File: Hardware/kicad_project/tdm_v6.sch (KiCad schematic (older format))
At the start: 34 parts, among them J4 DebugHeader, J5 USB_B_Micro, SW26 spst_4_pin_internal, SW27 spst_4_pin_internal, U1 W25Q32JVSS, U2 RP2040, Y1 Crystal

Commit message: update project with corrected schematic / pcb
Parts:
- removed J4: DebugHeader, Connector_PinSocket_2.54mm:PinSocket_1x04_P2.54mm_Vertical, symbol Connector:Conn_01x04_Female
- removed J5: USB_B_Micro, symbol Connector:USB_B_Micro
- removed Y1: Crystal, symbol Device:Crystal
- added C1: 1u, Capacitors_SMD:C_0402_NoSilk, symbol Device:C
- added J1: picoprobe_debug, RandomJunk:pico debug header, symbol customLibrary:picoprobe_debug
- added J2: USB_C_Receptacle_USB2.0, RandomJunk:USB-C_SMD-TYPE-C-31-M-12, symbol Connector:USB_C_Receptacle_USB2.0
- added R19, R20: 5.1k, Resistors_SMD:R_0402_NoSilk, symbol Device:R
- added Y1: Crystal_GND24, Crystals:Crystal_SMD_3225-4pin_3.2x2.5mm, symbol Device:Crystal_GND24
- C26: renamed from C39; footprint (none) -> Capacitors_SMD:C_0402_NoSilk; LCSC (none) -> C307331
- C27: renamed from C40; footprint (none) -> Capacitors_SMD:C_0402_NoSilk; LCSC (none) -> C307331
- C28: renamed from C41; footprint (none) -> Capacitors_SMD:C_0402_NoSilk; LCSC (none) -> C307331
- C29: renamed from C42; footprint (none) -> Capacitors_SMD:C_0402_NoSilk; LCSC (none) -> C307331
- C30: renamed from C43; footprint (none) -> Capacitors_SMD:C_0402_NoSilk; LCSC (none) -> C307331
- C31: renamed from C44; footprint (none) -> Capacitors_SMD:C_0402_NoSilk; LCSC (none) -> C307331
- C32: renamed from C45; footprint (none) -> Capacitors_SMD:C_0402_NoSilk; LCSC (none) -> C307331
- C33: renamed from C46; footprint (none) -> Capacitors_SMD:C_0402_NoSilk; LCSC (none) -> C52923
- C34: renamed from C49; footprint (none) -> Capacitors_SMD:C_0402_NoSilk; LCSC (none) -> C307331
- C35: renamed from C54; value 27p -> 30p; footprint (none) -> Capacitors_SMD:C_0402_NoSilk; LCSC (none) -> C1570
- C36: renamed from C57; footprint (none) -> Capacitors_SMD:C_0402_NoSilk; LCSC (none) -> C15525
- C37: renamed from C55; value 27p -> 30p; footprint (none) -> Capacitors_SMD:C_0402_NoSilk; LCSC (none) -> C1570
- R1: renamed from R7; footprint (none) -> Resistors_SMD:R_0402_NoSilk; LCSC (none) -> C31439
- R2: renamed from R8; footprint (none) -> Resistors_SMD:R_0402_NoSilk; LCSC (none) -> C31439
- R3: renamed from R9; footprint (none) -> Resistors_SMD:R_0402_NoSilk
- R4: renamed from R1; footprint Resistors_SMD:R_0603 -> Resistors_SMD:R_0402_NoSilk; LCSC c23162 -> C23162
- R5: renamed from R2; footprint Resistors_SMD:R_0603 -> Resistors_SMD:R_0402_NoSilk; LCSC c23162 -> C23162
- R6: renamed from R11; footprint (none) -> Resistors_SMD:R_0402_NoSilk; LCSC (none) -> C11702
- R7: renamed from R13; footprint (none) -> Resistors_SMD:R_0402_NoSilk; LCSC (none) -> C11702
- R8: renamed from R?; footprint Resistors_SMD:R_0603 -> Resistors_SMD:R_0402_NoSilk; LCSC c21190 -> C11702
- RV1, RV2: footprint RandomJunk:rk10j -> Potentiometers:Potentiometer_Alps_RK09K_Horizontal
- U1: footprint Package_SO:SOIC-8_5.23x5.23mm_P1.27mm -> Housings_SOIC:SOIJ-8_5.3x5.3mm_Pitch1.27mm; LCSC (none) -> C190862
- U2: footprint RP2040_minimal:RP2040-QFN-56 -> MCU_RaspberryPi_and_Boards:RP2040-QFN-56; LCSC (none) -> C2040
- gave numbers to parts that had none: 1
- renumbered SW27 to SW26, SW26 to SW27
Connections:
- net labels added: rx, swclk, swdio, tx
- wire segments 106 -> 129
- no-connect marks 1 -> 2
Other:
- moved on the sheet: C36

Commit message: initial firmware commit, update hardware
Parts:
- added C2, C3: 100n, Capacitors_SMD:C_0402_NoSilk, symbol Device:C
- R4, R5: LCSC C23162 -> C25900
- U1: LCSC C190862 -> C97521
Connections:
- net GND: now also C2.2, C3.2
- net at C1.1, U2.23 (DVDD), U2.45 (VREG_VOUT)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: now also C2.1, C3.1
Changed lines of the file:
@@
 F 2 "Resistors_SMD:R_0402_NoSilk" V 10340 2940 50  0001 C CNN
 F 3 "~" H 10300 2950 50  0001 C CNN
-F 4 "C23162" H 10300 2950 50  0001 C CNN "LCSC"
+F 4 "C25900" H 10300 2950 50  0001 C CNN "LCSC"
 	1    10300 2950
 	-1   0    0    -1
@@
 F 2 "Resistors_SMD:R_0402_NoSilk" V 10190 3040 50  0001 C CNN
 F 3 "~" H 10150 3050 50  0001 C CNN
-F 4 "C23162" H 10150 3050 50  0001 C CNN "LCSC"
+F 4 "C25900" H 10150 3050 50  0001 C CNN "LCSC"
 	1    10150 3050
 	-1   0    0    -1
@@
 F 2 "Housings_SOIC:SOIJ-8_5.3x5.3mm_Pitch1.27mm" H 5600 3300 50  0001 C CNN
 F 3 "http://www.winbond.com/resource-files/w25q32jv%20revg%2003272018%20plus.pdf" H 5600 3300 50  0001 C CNN
-F 4 "C190862" H 5600 3300 50  0001 C CNN "LCSC"
+F 4 "C97521" H 5600 3300 50  0001 C CNN "LCSC"
 	1    5600 3300
 	1    0    0    -1
@@
 	-1   0    0    -1
 $EndComp
+$Comp
+L Device:C C3
+U 1 1 61A2AB3F
+P 6850 2000
+F 0 "C3" H 6965 2046 50  0000 L CNN
+F 1 "100n" H 6965 1955 50  0000 L CNN
+F 2 "Capacitors_SMD:C_0402_NoSilk" H 6888 1850 50  0001 C CNN
+F 3 "~" H 6850 2000 50  0001 C CNN
+F 4 "C307331" H 6850 2000 50  0001 C CNN "LCSC"
+	1    6850 2000
+	1    0    0    -1
+$EndComp
+$Comp
+L Device:C C2
+U 1 1 61A2B7E8
+P 6550 2000
+F 0 "C2" H 6665 2046 50  0000 L CNN
+F 1 "100n" H 6665 1955 50  0000 L CNN
+F 2 "Capacitors_SMD:C_0402_NoSilk" H 6588 1850 50  0001 C CNN
+F 3 "~" H 6550 2000 50  0001 C CNN
+F 4 "C307331" H 6550 2000 50  0001 C CNN "LCSC"
+	1    6550 2000
+	1    0    0    -1
+$EndComp
+Wire Wire Line
+	7200 1800 6850 1800
+Wire Wire Line
+	6550 1800 6550 1850
+Connection ~ 7200 1800
+Wire Wire Line
+	6850 1800 6850 1850
+Connection ~ 6850 1800
+Wire Wire Line
+	6850 1800 6550 1800
+Wire Wire Line
+	6550 2150 6850 2150
+Connection ~ 7200 2150
+Connection ~ 6850 2150
+Wire Wire Line
+	6850 2150 7200 2150
 $EndSCHEMATC

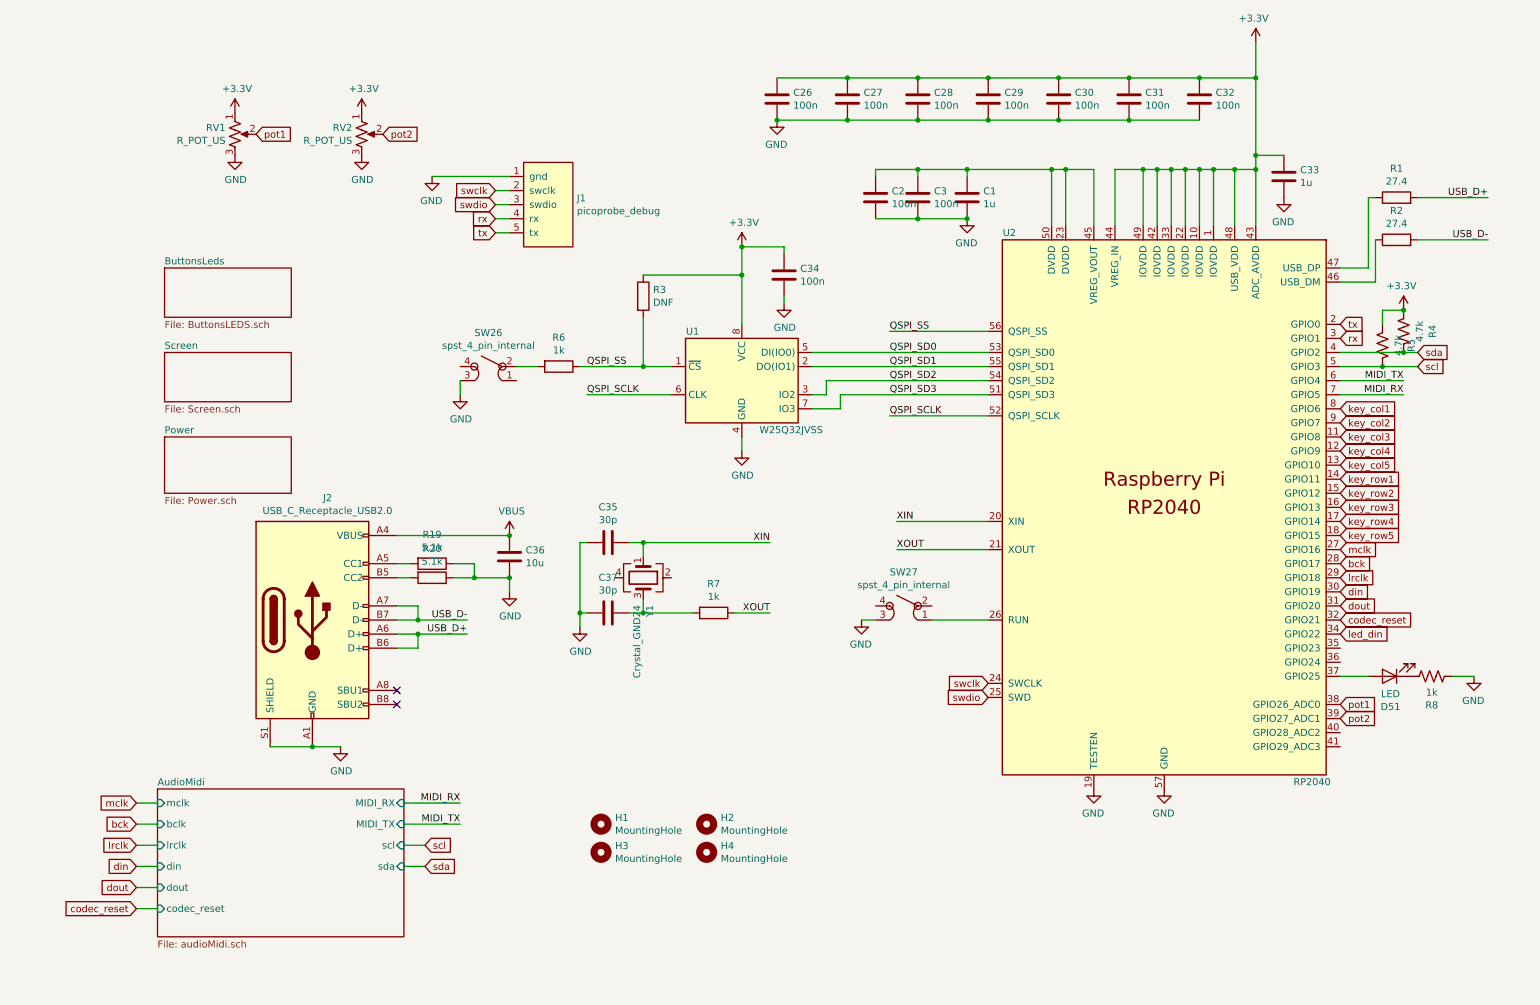
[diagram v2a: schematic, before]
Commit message: new hardware rev
- soft / latching power switch
- corrected mic
- added pullup to flash ss
- front & back enclosure plates
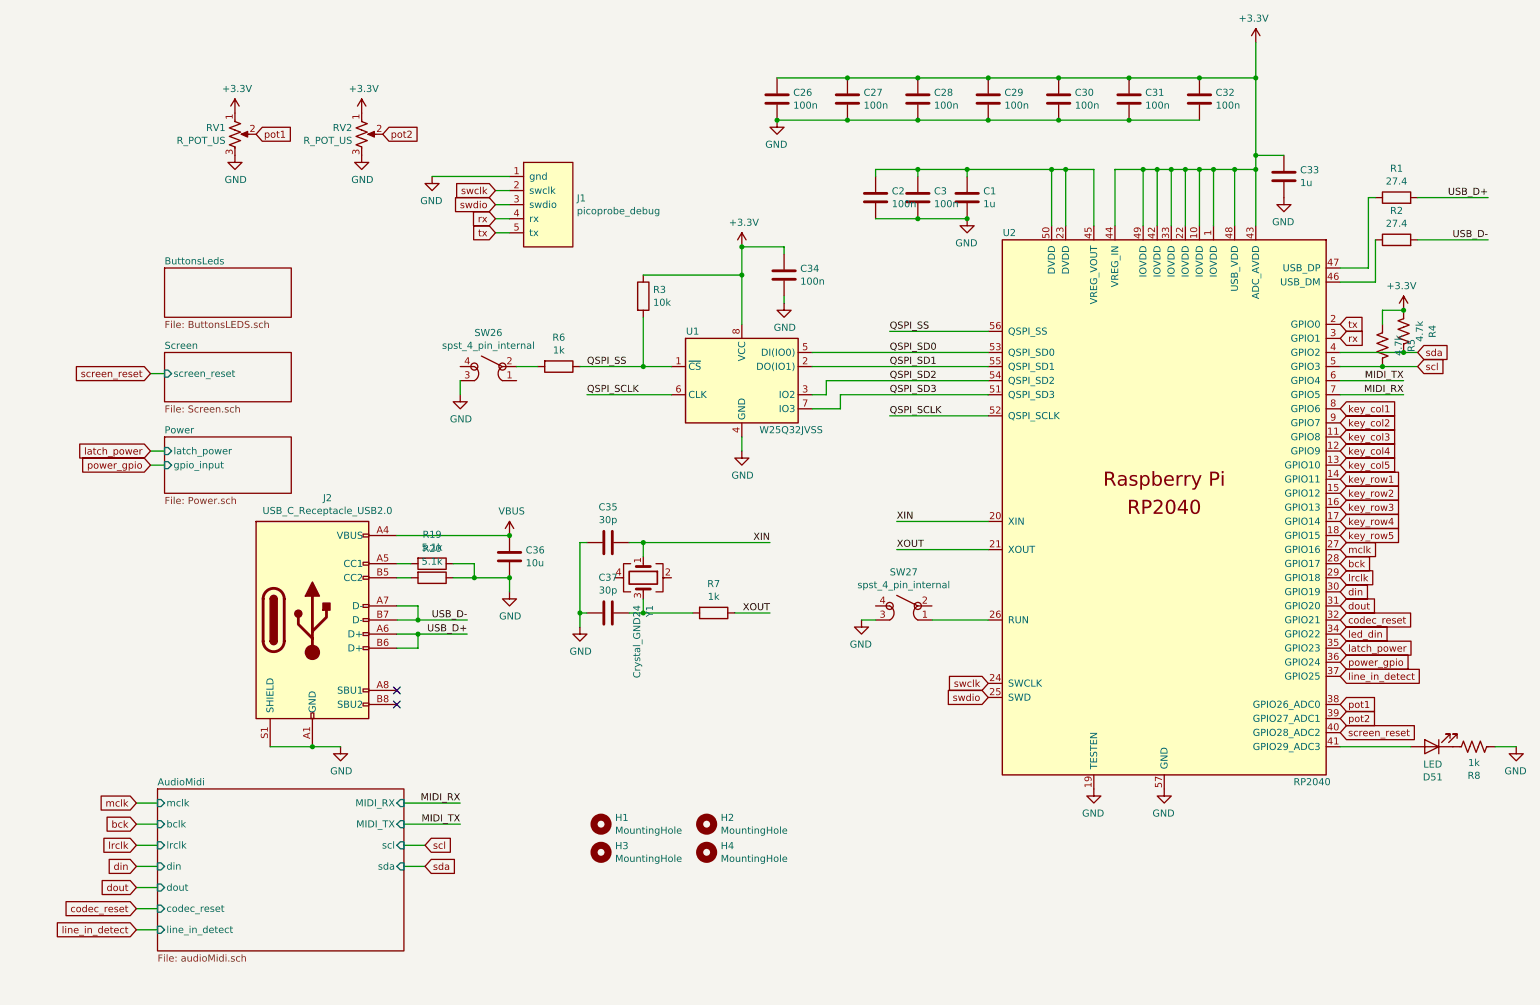
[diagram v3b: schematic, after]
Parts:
- R3: value DNF -> 10k; LCSC (none) -> C25744
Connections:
- net latch_power: now reaches U2.35 (GPIO23)
- net power_gpio: now reaches U2.36 (GPIO24)
- net at D51.2 (A): now also U2.41 (GPIO29_ADC3); no longer U2.37 (GPIO25)
- net screen_reset: now reaches U2.40 (GPIO28_ADC2)
- new net line_in_detect: U2.37 (GPIO25)
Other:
- moved on the sheet: D51, R8
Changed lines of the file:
@@
 P 4900 2700
 F 0 "R3" H 4970 2746 50  0000 L CNN
-F 1 "DNF" H 4970 2655 50  0000 L CNN
+F 1 "10k" H 4970 2655 50  0000 L CNN
 F 2 "Resistors_SMD:R_0402_NoSilk" V 4830 2700 50  0001 C CNN
 F 3 "~" H 4900 2700 50  0001 C CNN
+F 4 "C25744" H 4900 2700 50  0001 C CNN "LCSC"
 	1    4900 2700
 	1    0    0    -1
@@
 L Device:LED D51
 U 1 1 61FD1144
-P 10200 5400
-F 0 "D51" H 10193 5616 50  0000 C CNN
-F 1 "LED" H 10193 5525 50  0000 C CNN
-F 2 "LEDs:LED_0603" H 10200 5400 50  0001 C CNN
-F 3 "~" H 10200 5400 50  0001 C CNN
-F 4 "c2286" H 10200 5400 50  0001 C CNN "LCSC"
-	1    10200 5400
+P 10500 5900
+F 0 "D51" H 10493 6116 50  0000 C CNN
+F 1 "LED" H 10493 6025 50  0000 C CNN
+F 2 "LEDs:LED_0603" H 10500 5900 50  0001 C CNN
+F 3 "~" H 10500 5900 50  0001 C CNN
+F 4 "c2286" H 10500 5900 50  0001 C CNN "LCSC"
+	1    10500 5900
 	-1   0    0    1
 $EndComp
@@
 L Device:R_US R8
 U 1 1 61FD114B
-P 10500 5400
-F 0 "R8" V 10295 5400 50  0000 C CNN
-F 1 "1k" V 10386 5400 50  0000 C CNN
-F 2 "Resistors_SMD:R_0402_NoSilk" V 10540 5390 50  0001 C CNN
-F 3 "~" H 10500 5400 50  0001 C CNN
-F 4 "C11702" H 10500 5400 50  0001 C CNN "LCSC"
-	1    10500 5400
+P 10800 5900
+F 0 "R8" V 10595 5900 50  0000 C CNN
+F 1 "1k" V 10686 5900 50  0000 C CNN
+F 2 "Resistors_SMD:R_0402_NoSilk" V 10840 5890 50  0001 C CNN
+F 3 "~" H 10800 5900 50  0001 C CNN
+F 4 "C11702" H 10800 5900 50  0001 C CNN "LCSC"
+	1    10800 5900
 	0    -1   -1   0
 $EndComp
-Wire Wire Line
-	9850 5400 10050 5400
 $Comp
 L power:GND #PWR019
 U 1 1 6204155A
-P 10800 5400
-F 0 "#PWR019" H 10800 5150 50  0001 C CNN
-F 1 "GND" H 10805 5227 50  0000 C CNN
-F 2 "" H 10800 5400 50  0001 C CNN
-F 3 "" H 10800 5400 50  0001 C CNN
-	1    10800 5400
+P 11100 5900
+F 0 "#PWR019" H 11100 5650 50  0001 C CNN
+F 1 "GND" H 11105 5727 50  0000 C CNN
+F 2 "" H 11100 5900 50  0001 C CNN
+F 3 "" H 11100 5900 50  0001 C CNN
+	1    11100 5900
 	-1   0    0    -1
 $EndComp
 Wire Wire Line
-	10650 5400 10800 5400
+	10950 5900 11100 5900
 Wire Wire Line
 	9250 900  9250 1150
@@
 	3200 6450 3600 6450
 $Sheet
-S 1450 6200 1750 1050
+S 1450 6200 1750 1150
 U 62E6C628
 F0 "AudioMidi" 50
@@
 F10 "scl" I R 3200 6600 50
 F11 "sda" I R 3200 6750 50
+F12 "line_in_detect" I L 1450 7200 50
 $EndSheet
 $Sheet
@@
 F0 "Screen" 50
 F1 "Screen.sch" 50
+F2 "screen_reset" I L 1500 3250 50
 $EndSheet
 $Sheet
@@
 F0 "Power" 50
 F1 "Power.sch" 50
+F2 "latch_power" I L 1500 3800 50
+F3 "gpio_input" I L 1500 3900 50
 $EndSheet
 $Comp
@@
 Wire Wire Line
 	6850 2150 7200 2150
+Text GLabel 1400 3800 0    50   Input ~ 0
+latch_power
+Text GLabel 1400 3900 0    50   Input ~ 0
+power_gpio
+Text GLabel 1400 3250 0    50   Input ~ 0
+screen_reset
+Text GLabel 9850 5300 2    50   Input ~ 0
+power_gpio
+Text GLabel 9850 5800 2    50   Input ~ 0
+screen_reset
+Wire Wire Line
+	1400 3250 1500 3250
+Wire Wire Line
+	1400 3800 1500 3800
+Wire Wire Line
+	1400 3900 1500 3900
+Text GLabel 1300 7200 0    50   Input ~ 0
+line_in_detect
+Wire Wire Line
+	1300 7200 1450 7200
+Text GLabel 9850 5400 2    50   Input ~ 0
+line_in_detect
+Text GLabel 9850 5200 2    50   Input ~ 0
+latch_power
+Wire Wire Line
+	9850 5900 10350 5900
 $EndSCHEMATC

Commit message: corrected some hardware issues.
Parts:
- RV1, RV2: LCSC (none) -> C209779
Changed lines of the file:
@@
 F 2 "Potentiometers:Potentiometer_Alps_RK09K_Horizontal" H 2000 1550 50  0001 C CNN
 F 3 "~" H 2000 1550 50  0001 C CNN
+F 4 "C209779" H 2000 1550 50  0001 C CNN "LCSC"
 	1    2000 1550
 	1    0    0    -1
@@
 F 2 "Potentiometers:Potentiometer_Alps_RK09K_Horizontal" H 2900 1550 50  0001 C CNN
 F 3 "~" H 2900 1550 50  0001 C CNN
+F 4 "C209779" H 2900 1550 50  0001 C CNN "LCSC"
 	1    2900 1550
 	1    0    0    -1
